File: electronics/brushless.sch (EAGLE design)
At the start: 70 parts, among them J1 USB_MINI-B_SMT, Q1 BUK7Y12-40E, Q2 BUK7Y12-40E, Q3 BUK7Y12-40E, Q4 BUK7Y12-40E, Q5 BUK7Y12-40E, Q6 BUK7Y12-40E, X1 JST-XH-10-PIN-LONG-PAD

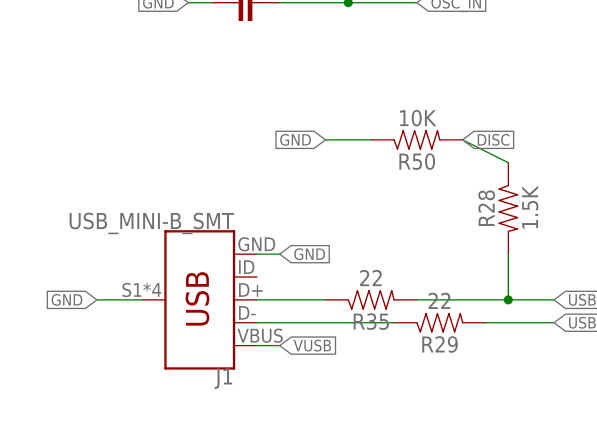
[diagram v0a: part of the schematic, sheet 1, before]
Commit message: Moving to vertical micro usb connector, adding silk
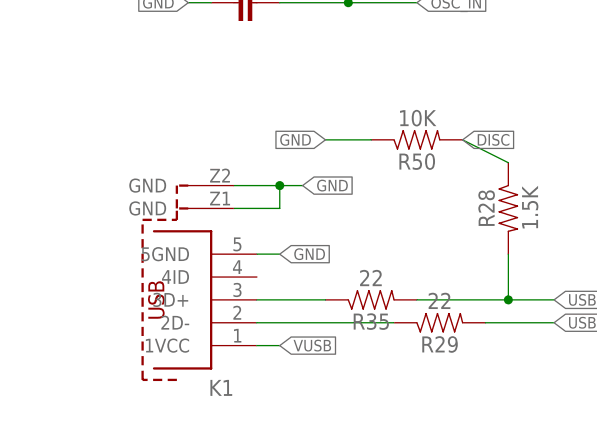
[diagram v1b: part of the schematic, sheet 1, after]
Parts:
- removed J1: USB_MINI-B_SMT, SparkFun-Connectors:USB_MINI-B_SMT
- added K1: (no value), Wurth_Input-Output_Connectors_rev15d:614105150721
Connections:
- net GND: now also K1.5GND, K1.GND@1, K1.GND@2; no longer J1.GND, J1.SHIELD
- net N$59: now also K1.2D-; no longer J1.D-
- net N$60: now also K1.3D+; no longer J1.D+
- net VUSB: now also K1.1VCC; no longer J1.VBUS
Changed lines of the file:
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@@
 <class number="0" name="default" width="0" drill="0">
+</class>
+<class number="1" name="vdriver" width="0.254" drill="0">
 </class>
 <class number="2" name="power" width="0" drill="0">
@@
 <attribute name="FARNELL" value="2496946"/>
 </part>
-<part name="J1" library="SparkFun-Connectors" deviceset="USB_MINI-B" device="_SMT">
-<attribute name="FARNELL" value="1753807"/>
-</part>
 <part name="DRV1" library="rhoban" deviceset="OPEN-BLDC_IR2101" device="">
 <attribute name="FARNELL" value="2296000"/>
@@
 <part name="C10" library="rhoban" deviceset="CPOL_EU" device="_3.5-8" value="100uF">
 <attribute name="FARNELL" value="1144713"/>
+</part>
+<part name="K1" library="Wurth_Input-Output_Connectors_rev15d" deviceset="614105150721" device="">
+<attribute name="FARNELL" value="2470830"/>
 </part>
 </parts>
@@
 <attribute name="FARNELL" x="66.04" y="43.18" size="1.778" layer="96" rot="R180" display="off"/>
 </instance>
-<instance part="J1" gate="G$1" x="-48.26" y="-48.26" rot="R180">
-<attribute name="FARNELL" x="-48.26" y="-48.26" size="1.778" layer="96" rot="R180" display="off"/>
+<instance part="K1" gate="G$1" x="-50.8" y="-48.26" rot="R180">
+<attribute name="FARNELL" x="-50.8" y="-48.26" size="1.778" layer="96" rot="R180" display="off"/>
 </instance>
 </instances>
@@
 <segment>
 <label x="-40.64" y="-43.18" size="1.27" layer="95" xref="yes"/>
-<pinref part="J1" gate="G$1" pin="GND"/>
 <wire x1="-40.64" y1="-43.18" x2="-43.18" y2="-43.18" width="0.1524" layer="91"/>
+<pinref part="K1" gate="G$1" pin="5GND"/>
 </segment>
 <segment>
@@
 </segment>
 <segment>
-<pinref part="J1" gate="G$1" pin="SHIELD"/>
-<wire x1="-55.88" y1="-48.26" x2="-60.96" y2="-48.26" width="0.1524" layer="91"/>
-<label x="-60.96" y="-48.26" size="1.27" layer="95" rot="R180" xref="yes"/>
+<pinref part="K1" gate="G$1" pin="GND@2"/>
+<wire x1="-45.72" y1="-35.56" x2="-40.64" y2="-35.56" width="0.1524" layer="91"/>
+<pinref part="K1" gate="G$1" pin="GND@1"/>
+<wire x1="-45.72" y1="-38.1" x2="-40.64" y2="-38.1" width="0.1524" layer="91"/>
+<wire x1="-40.64" y1="-38.1" x2="-40.64" y2="-35.56" width="0.1524" layer="91"/>
+<wire x1="-40.64" y1="-35.56" x2="-38.1" y2="-35.56" width="0.1524" layer="91"/>
+<label x="-38.1" y="-35.56" size="1.27" layer="95" xref="yes"/>
+<junction x="-40.64" y="-35.56"/>
 </segment>
 </net>
@@
 <segment>
 <label x="-40.64" y="-53.34" size="1.27" layer="95" xref="yes"/>
-<pinref part="J1" gate="G$1" pin="VBUS"/>
 <wire x1="-43.18" y1="-53.34" x2="-40.64" y2="-53.34" width="0.1524" layer="91"/>
+<pinref part="K1" gate="G$1" pin="1VCC"/>
 </segment>
 </net>
@@
 <segment>
 <pinref part="R29" gate="G$1" pin="1"/>
-<pinref part="J1" gate="G$1" pin="D-"/>
 <wire x1="-43.18" y1="-50.8" x2="-27.94" y2="-50.8" width="0.1524" layer="91"/>
+<pinref part="K1" gate="G$1" pin="2D-"/>
 </segment>
 </net>
@@
 <wire x1="-43.18" y1="-48.26" x2="-35.56" y2="-48.26" width="0.1524" layer="91"/>
 <pinref part="R35" gate="G$1" pin="1"/>
-<pinref part="J1" gate="G$1" pin="D+"/>
+<pinref part="K1" gate="G$1" pin="3D+"/>
 </segment>
 </net>
@@
 </segment>
 </net>
-<net name="VDRIVER" class="0">
+<net name="VDRIVER" class="1">
 <segment>
 <pinref part="DRV1" gate="G$1" pin="VCC"/>
@@
 </segment>
 </net>
-<net name="VDRIVER" class="0">
+<net name="VDRIVER" class="1">
 <segment>
 <wire x1="71.12" y1="-22.86" x2="63.5" y2="-22.86" width="0.1524" layer="91"/>

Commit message: Brushless board
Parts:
- removed R13: 0Ohm, rhoban:RESISTANCE-R0805
- added D5: (no value), SparkFun-DiscreteSemi:DIODESOD
- added JP1, JP2: JUMPER-SMT_2_NO_NO-SILK_ROUND, SparkFun-Jumpers:JUMPER-SMT_2_NO_NO-SILK_ROUND
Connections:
- new net N$22: JP2.2, REG1.IN
- net V+: now also JP1.1; no longer R13.1
- net VCC: now also D5.C, JP2.1; no longer REG1.IN
- net VDRIVER: now also JP1.2; no longer R13.2
- net VUSB: now also D5.A
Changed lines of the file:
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@@
 <attribute name="FARNELL" value="2528772"/>
-</part>
-<part name="R13" library="rhoban" deviceset="RESISTANCE" device="-R0805" value="0Ohm">
-<attribute name="FARNELL" value="-"/>
 </part>
 <part name="R1" library="SparkFun-Resistors" deviceset="RESISTOR" device="0805" value="1K">
@@
 <part name="K1" library="Wurth_Input-Output_Connectors_rev15d" deviceset="614105150721" device="">
 <attribute name="FARNELL" value="2470830"/>
+</part>
+<part name="D5" library="SparkFun-DiscreteSemi" deviceset="DIODE" device="SOD">
+<attribute name="FARNELL" value="8737843RL"/>
+</part>
+<part name="JP1" library="SparkFun-Jumpers" deviceset="JUMPER-SMT_2_NO" device="_NO-SILK_ROUND">
+<attribute name="FARNELL" value="-"/>
+</part>
+<part name="JP2" library="SparkFun-Jumpers" deviceset="JUMPER-SMT_2_NO" device="_NO-SILK_ROUND">
+<attribute name="FARNELL" value="-"/>
 </part>
 </parts>
@@
 <instance part="K1" gate="G$1" x="-50.8" y="-48.26" rot="R180">
 <attribute name="FARNELL" x="-50.8" y="-48.26" size="1.778" layer="96" rot="R180" display="off"/>
+</instance>
+<instance part="D5" gate="G$1" x="-40.64" y="-55.88" rot="R270">
+<attribute name="FARNELL" x="-40.64" y="-55.88" size="1.27" layer="96" rot="R270" display="off"/>
 </instance>
 </instances>
@@
 <net name="VUSB" class="0">
 <segment>
-<label x="-40.64" y="-53.34" size="1.27" layer="95" xref="yes"/>
+<label x="-38.1" y="-53.34" size="1.27" layer="95" xref="yes"/>
 <wire x1="-43.18" y1="-53.34" x2="-40.64" y2="-53.34" width="0.1524" layer="91"/>
 <pinref part="K1" gate="G$1" pin="1VCC"/>
+<pinref part="D5" gate="G$1" pin="A"/>
+<junction x="-40.64" y="-53.34"/>
+<wire x1="-40.64" y1="-53.34" x2="-38.1" y2="-53.34" width="0.1524" layer="91"/>
 </segment>
 </net>
@@
 </segment>
 </net>
+<net name="VCC" class="0">
+<segment>
+<pinref part="D5" gate="G$1" pin="C"/>
+<wire x1="-40.64" y1="-58.42" x2="-40.64" y2="-60.96" width="0.1524" layer="91"/>
+<wire x1="-40.64" y1="-60.96" x2="-38.1" y2="-63.5" width="0.1524" layer="91"/>
+<label x="-38.1" y="-63.5" size="1.27" layer="95" xref="yes"/>
+</segment>
+</net>
 </nets>
 </sheet>
@@
 <attribute name="FARNELL" x="88.9" y="22.86" size="1.778" layer="96" display="off"/>
 </instance>
-<instance part="R13" gate="G$1" x="53.34" y="0">
-<attribute name="FARNELL" x="53.34" y="0" size="1.778" layer="96" display="off"/>
+<instance part="JP1" gate="G$1" x="53.34" y="0">
+<attribute name="FARNELL" x="53.34" y="0" size="1.27" layer="96" display="off"/>
 </instance>
 </instances>
@@
 </segment>
 </net>
-<net name="V+" class="2">
-<segment>
-<pinref part="R13" gate="G$1" pin="1"/>
+<net name="V+" class="1">
+<segment>
 <wire x1="48.26" y1="0" x2="45.72" y2="0" width="0.1524" layer="91"/>
 <label x="45.72" y="0" size="1.27" layer="95" rot="R180" xref="yes"/>
+<pinref part="JP1" gate="G$1" pin="1"/>
 </segment>
 </net>
@@
 </segment>
 <segment>
-<pinref part="R13" gate="G$1" pin="2"/>
 <wire x1="58.42" y1="0" x2="60.96" y2="0" width="0.1524" layer="91"/>
 <label x="60.96" y="0" size="1.27" layer="95" xref="yes"/>
+<pinref part="JP1" gate="G$1" pin="2"/>
 </segment>
 </net>
@@
 </segment>
 </net>
-<net name="V+" class="2">
+<net name="V+" class="1">
 <segment>
 <wire x1="71.12" y1="83.82" x2="71.12" y2="88.9" width="0.1524" layer="91"/>
@@
 <attribute name="FARNELL" x="33.02" y="-30.48" size="1.778" layer="96" display="off"/>
 </instance>
+<instance part="JP2" gate="G$1" x="-15.24" y="-25.4">
+<attribute name="FARNELL" x="-15.24" y="-25.4" size="1.27" layer="96" display="off"/>
+</instance>
 </instances>
 <busses>
@@
 </segment>
 <segment>
-<pinref part="REG1" gate="G$1" pin="IN"/>
-<wire x1="-7.62" y1="-25.4" x2="-10.16" y2="-25.4" width="0.1524" layer="91"/>
-<label x="-10.16" y="-25.4" size="1.27" layer="95" rot="R180" xref="yes"/>
+<pinref part="JP2" gate="G$1" pin="1"/>
+<wire x1="-20.32" y1="-25.4" x2="-22.86" y2="-25.4" width="0.1524" layer="91"/>
+<label x="-22.86" y="-25.4" size="1.27" layer="95" rot="R180" xref="yes"/>
 </segment>
 </net>
@@
 </segment>
 </net>
-<net name="V+" class="2">
+<net name="V+" class="1">
 <segment>
 <pinref part="V+" gate="G$1" pin="3"/>
@@
 </segment>
 </net>
+<net name="N$22" class="0">
+<segment>
+<pinref part="REG1" gate="G$1" pin="IN"/>
+<wire x1="-7.62" y1="-25.4" x2="-10.16" y2="-25.4" width="0.1524" layer="91"/>
+<pinref part="JP2" gate="G$1" pin="2"/>
+<wire x1="-10.16" y1="-25.4" x2="-12.7" y2="-25.4" width="0.1524" layer="91"/>
+<junction x="-10.16" y="-25.4"/>
+</segment>
+</net>
